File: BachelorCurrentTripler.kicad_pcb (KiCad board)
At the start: 4 copper layers, 153.3 x 77.8 mm, 80 parts, among them J1 Conn_01x07_Pin, J2 Conn_01x01_Pin, J3 Conn_01x01_Pin, J5 Conn_01x01_Pin, J6 Conn_01x01_Pin, J7 Conn_01x01_Pin, Q10 IRLR8726EBF, Q11 IRLR8726EBF, Q13 C2M0025120D, Q14 C2M0025120D, Q15 C2M0025120D, Q16 C2M0025120D, Q7 C2M0025120D, Q8 C2M0025120D, Q9 IRLR8726EBF, U1 STDriveG600, U2 STDriveG600, U3 STDriveG600, U4 FAN3268, U5 FAN3268, U6 FAN3268

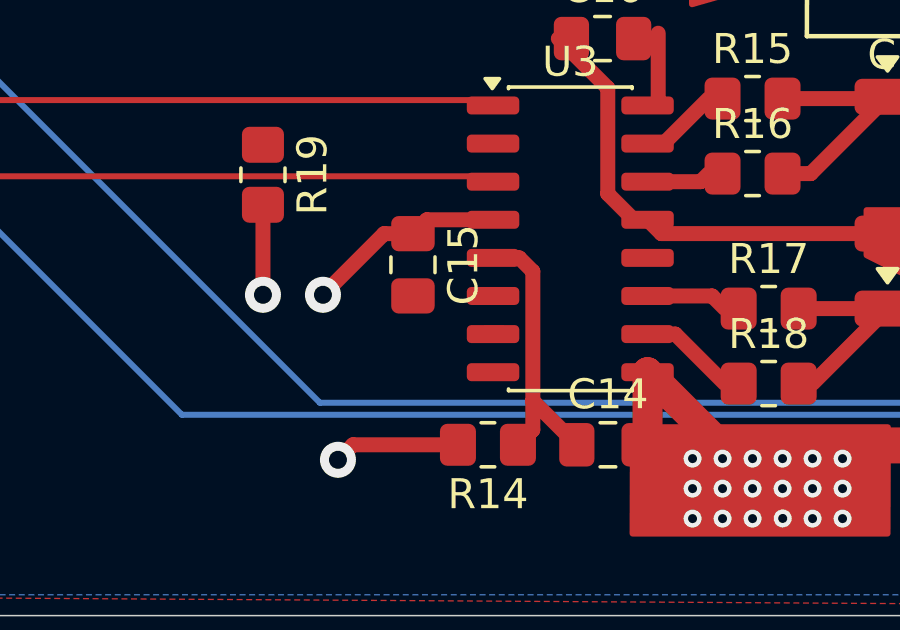
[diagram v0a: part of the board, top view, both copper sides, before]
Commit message: Small addition to GND on primary side
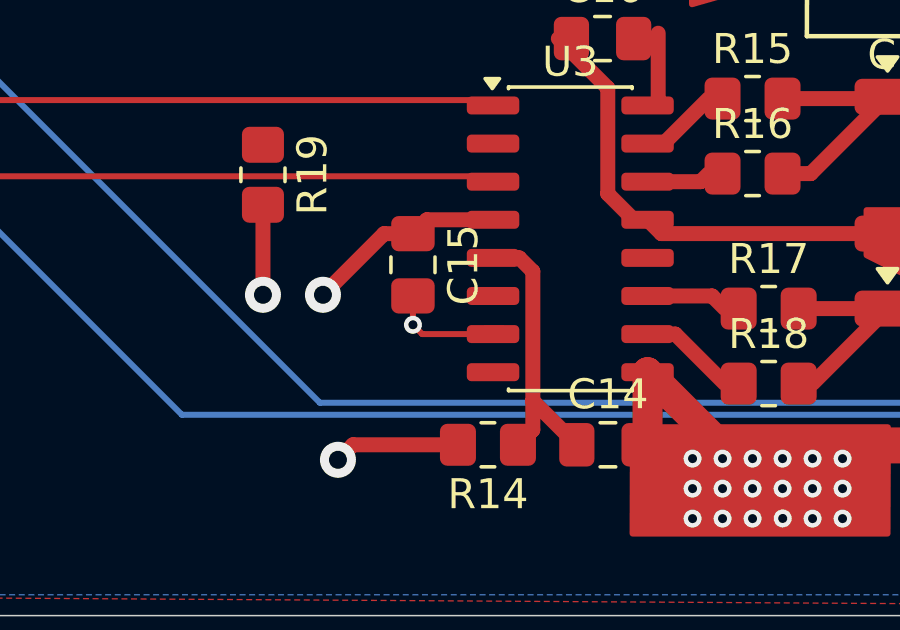
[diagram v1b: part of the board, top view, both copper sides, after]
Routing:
- net GND: track 53.8 -> 57.6 mm, vias 125 -> 126
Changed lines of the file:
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@@
+	)
+	(segment
+		(start 117.81 133.81)
+		(end 120.17 133.81)
+		(width 0.2)
+		(layer "F.Cu")
+		(net 1)
 	)
 	(segment
@@
 	)
 	(segment
+		(start 117.5 133.5)
+		(end 117.5 132.5375)
+		(width 0.2)
+		(layer "F.Cu")
+		(net 1)
+	)
+	(segment
 		(start 207.5375 120.5375)
 		(end 208.5 121.5)
@@
 	)
 	(segment
+		(start 117.5 133.5)
+		(end 117.81 133.81)
+		(width 0.2)
+		(layer "F.Cu")
+		(net 1)
+	)
+	(segment
 		(start 207.5375 120.5)
 		(end 207.5375 120.5375)
@@
 		(size 0.6)
 		(drill 0.3)
+		(layers "F.Cu" "B.Cu")
+		(net 1)
+	)
+	(via
+		(at 117.5 133.5)
+		(size 0.6)
+		(drill 0.3)

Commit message: Secondary side finished
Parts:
- added C36: C, Capacitor_THT:CP_Radial_D8.0mm_P5.00mm, F.Cu at (105.5, 91.5)
- added C37: C, Capacitor_THT:CP_Radial_D8.0mm_P5.00mm, F.Cu at (105.5, 77.6)
- moved C21 36.2 mm to (214.0, 116.6), turned to -90 degrees
- moved C26 34.3 mm to (202.0, 121.5), turned to -90 degrees
- moved C24 33.1 mm to (204.0, 121.5), turned to -90 degrees
- moved C23 27.9 mm to (202.0, 106.5), turned to -90 degrees
- moved C22 26.4 mm to (204.0, 106.5), turned to -90 degrees
- moved C20 18.9 mm to (214.0, 101.6), turned to -90 degrees
- moved C28 11.8 mm to (223.0, 102.6), turned to -90 degrees
- moved J3 11.5 mm to (91.0, 96.5)
- moved C25 10.4 mm to (204.0, 91.5), turned to -90 degrees
- moved C27 10.3 mm to (202.0, 91.5), turned to -90 degrees
- moved J5 9.05 mm to (91.5, 85.5)
- moved C29 7.83 mm to (214.5, 86.1), turned to -90 degrees
- moved C33 2.00 mm to (208.0, 90.5)
- moved C30 1.50 mm to (208.0, 92.5)
- moved R21 1.41 mm to (202.5, 112.5), turned to 180 degrees
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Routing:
- net /PhaseA/ALin: track 45.6 -> 226.2 mm, vias 0 -> 1
- net +12V: track 191.2 -> 337.7 mm, vias 29 -> 35
- net +1V2: track 0.00 -> 112.2 mm
- net /PhaseB/BLIN: track 147.9 -> 189.8 mm, vias 0 -> 1
- net /PhaseC/CLIN: track 142.2 -> 173.6 mm, vias 0 -> 1
- net /SecondarySide/SecA: track 27.9 -> 55.9 mm
- net /SecondarySide/SecB: track 5.00 -> 28.8 mm
- net GND: track 57.6 -> 34.3 mm, vias 126 -> 279
- net /PhaseC/COUT: track 47.4 -> 70.3 mm
- net /SecondarySide/SecC: track 5.00 -> 25.3 mm
- net /PhaseB/BOUT: track 35.2 -> 53.7 mm
- net /PhaseA/AOUT: track 59.7 -> 67.5 mm
- net /PhaseA/AHin: track 44.1 -> 51.7 mm
- net +48V: track 192.1 -> 195.0 mm
- net Net-(U4-OUTA): track 4.47 -> 2.48 mm
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
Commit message: Rettelser efter møde med Andreas
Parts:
- added H1: MountingHole_Pad, MountingHole:MountingHole_4.3mm_M4_Pad_Via, F.Cu at (227.8, 73.2)
- added H2: MountingHole_Pad, MountingHole:MountingHole_4.3mm_M4_Pad_Via, F.Cu at (227.8, 136.2)
- added H3: MountingHole_Pad, MountingHole:MountingHole_4.3mm_M4_Pad_Via, F.Cu at (113.5, 70.2)
- added H4: MountingHole_Pad, MountingHole:MountingHole_4.3mm_M4_Pad_Via, F.Cu at (92.0, 136.2)
- Q10, Q11, Q9: moved to B.Cu
- moved Q9 6.65 mm to (200.6, 96.5), turned to 0 degrees
- moved Q11 6.40 mm to (200.5, 124.7), turned to 0 degrees
- moved Q10 5.91 mm to (200.1, 110.2), turned to 0 degrees
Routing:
- net /SecondarySide/SecA: track 55.9 -> 82.1 mm, vias 0 -> 21
- net /SecondarySide/SecC: track 25.3 -> 34.1 mm, vias 0 -> 11
- net Net-(Q10-G): track 2.30 -> 6.47 mm, vias 0 -> 1
- net Net-(Q9-G): track 2.61 -> 6.39 mm, vias 0 -> 1
- net /PhaseA/ALin: track 226.2 -> 222.5 mm
- net Net-(Q11-G): track 2.57 -> 6.00 mm, vias 0 -> 1
- net /SecondarySide/SecB: track 28.8 -> 32.2 mm, vias 0 -> 18
- net /PhaseB/BLIN: track 189.8 -> 186.8 mm
- net GND: track 34.3 -> 33.5 mm, vias 279 -> 274
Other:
- outline, holes or cut-outs redrawn
- board text added: "0 mm"
- board text added: "10 mm"
- board text added: "20 mm"
- board text added: "30 mm"
- board text added: "40 mm"
- board text added: "HUSK PUNKT TIL FEEDBACK SPÆNDING"
- board text removed: "kør ikke strøm under"

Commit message: burde være færdig nu
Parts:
- added J8: Conn_01x02_Pin, Connector:JWT_A3963_1x02_P3.96mm_Vertical, F.Cu at (214.1, 136.5)
- moved H3 0.56 mm to (113.5, 70.8)
- moved R12 0.17 mm to (116.0, 106.2)
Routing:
- net +1V2: track 112.2 -> 148.4 mm
- net Net-(U3-SD): track 0.19 -> 7.88 mm
- net GND: track 33.5 -> 35.5 mm, vias 274 -> 286
- net /SecondarySide/SecC: vias 11 -> 12
- net +48V: vias 117 -> 115
- added copper zone on F.Cu, net +1V2
- added copper zone on B.Cu, net /SecondarySide/SecA
- added copper zone on F.Cu, net /SecondarySide/SecA
- added copper zone on B.Cu, net /SecondarySide/SecB
- added copper zone on B.Cu, net /SecondarySide/SecC
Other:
- board text added: "Vsense"
- board text removed: "J2"
- board text removed: "Stor kondensator mellem 48V og GND men også 12V og GND"
- board text removed: "byt"

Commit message: tilføj lige sidste markeringer
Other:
- board text added: "1V2"
- board text added: "AH"
- board text added: "AL"
- board text added: "BH"
- board text added: "BL"
- board text added: "CH"
- board text added: "CL"
- board text removed: "HUSK PUNKT TIL FEEDBACK SPÆNDING"
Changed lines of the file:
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@@
 		(embedded_fonts no)
 		(model "${KICAD9_3DMODEL_DIR}/Transformer_THT.3dshapes/Transformer_Breve_TEZ-47x57.step"
+			(hide yes)
 			(offset
 				(xyz 0 0 0)
@@
 		(tags "connector JST EH vertical")
 		(property "Reference" "J1"
-			(at 7.5 -2.8 90)
+			(at 7.5 3.3 90)
 			(layer "F.SilkS")
 			(effects
@@
 		(layer "Edge.Cuts")
 	)
-	(gr_text "HUSK PUNKT TIL FEEDBACK SPÆNDING"
-		(at 239.5 94 0)
-		(layer "F.Cu")
+	(gr_text "20 mm"
+		(at 186 75 270)
+		(layer "F.SilkS")
 		(effects
 			(font
-				(size 1.5 1.5)
-				(thickness 0.3)
-				(bold yes)
+				(size 1 1)
+				(thickness 0.1)
 			)
 			(justify left bottom)
 		)
 	)
-	(gr_text "20 mm"
-		(at 186 75 270)
+	(gr_text "AL"
+		(at 93 108 0)
+		(layer "F.SilkS")
+		(effects
+			(font
+				(size 1 1)
+				(thickness 0.1)
+			)
+			(justify left bottom)
+		)
+	)
+	(gr_text "AH"
+		(at 93 110.5 0)
 		(layer "F.SilkS")
 		(effects
@@
 		)
 	)
+	(gr_text "BL"
+		(at 93 113 0)
+		(layer "F.SilkS")
+		(effects
+			(font
+				(size 1 1)
+				(thickness 0.1)
+			)
+			(justify left bottom)
+		)
+	)
 	(gr_text "30 mm"
 		(at 196 75 270)
@@
 		)
 	)
+	(gr_text "CH"
+		(at 93 120.5 0)
+		(layer "F.SilkS")
+		(effects
+			(font
+				(size 1 1)
+				(thickness 0.1)
+			)
+			(justify left bottom)
+		)
+	)
+	(gr_text "1V2"
+		(at 230 96 0)
+		(layer "F.SilkS")
+		(effects
+			(font
+				(size 2 2)
+				(thickness 0.1)
+			)
+			(justify left bottom)
+		)
+	)
+	(gr_text "GND"
+		(at 93 123 0)
+		(layer "F.SilkS")
+		(effects
+			(font
+				(size 1 1)
+				(thickness 0.1)
+			)
+			(justify left bottom)
+		)
+	)
+	(gr_text "CL"
+		(at 93 118 0)
+		(layer "F.SilkS")
+		(effects
+			(font
+				(size 1 1)
+				(thickness 0.1)
+			)
+			(justify left bottom)
+		)
+	)
 	(gr_text "10-15V max"
 		(at 87 93.5 0)
@@
 		)
 	)
+	(gr_text "BH"
+		(at 93 115.5 0)
+		(layer "F.SilkS")
+		(effects
+			(font
+				(size 1 1)
+				(thickness 0.1)
+			)
+			(justify left bottom)
+		)
+	)
 	(gr_text "40 mm"
 		(at 206 75 270)
@@
 				(thickness 0.1)
 			)
+			(justify left bottom)
+		)
+	)
+	(gr_text "GND"
+		(at 229.5 114.5 0)
+		(layer "F.SilkS")
+		(effects
+			(font
+				(size 2 2)
+				(thickness 0.1)
+			)

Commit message: Final Value Changes
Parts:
- C20, C29: value 220u -> 100u
- C28: value 100u -> 220u
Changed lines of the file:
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@@
 			)
 		)
-		(property "Value" "220u"
+		(property "Value" "100u"
 			(at -4 0 90)
 			(layer "F.Fab")
@@
 			)
 		)
-		(property "Value" "220u"
+		(property "Value" "100u"
 			(at 2.5 5.25 90)
 			(layer "F.Fab")
@@
 			)
 		)
-		(property "Value" "100u"
+		(property "Value" "220u"
 			(at 2.5 5.25 90)
 			(layer "F.Fab")
@@
 		(min_thickness 0.25)
 		(filled_areas_thickness no)
-		(fill yes
+		(fill
 			(thermal_gap 0.5)
 			(thermal_bridge_width 0.5)
@@
 		(min_thickness 0.25)
 		(filled_areas_thickness no)
-		(fill yes
+		(fill
 			(thermal_gap 0.5)
 			(thermal_bridge_width 0.5)
@@
 		(min_thickness 0.25)
 		(filled_areas_thickness no)
-		(fill yes
+		(fill
 			(thermal_gap 0.5)
 			(thermal_bridge_width 0.5)
@@
 		(min_thickness 0.25)
 		(filled_areas_thickness no)
-		(fill yes
+		(fill
 			(thermal_gap 0.5)
 			(thermal_bridge_width 0.5)
@@
 		(min_thickness 0.25)
 		(filled_areas_thickness no)
-		(fill yes
+		(fill
 			(thermal_gap 0.5)
 			(thermal_bridge_width 0.5)
@@
 		(min_thickness 0.25)
 		(filled_areas_thickness no)
-		(fill yes
+		(fill
 			(thermal_gap 0.5)
 			(thermal_bridge_width 0.5)
@@
 		(min_thickness 0.25)
 		(filled_areas_thickness no)
-		(fill yes
+		(fill
 			(thermal_gap 0.5)
 			(thermal_bridge_width 0.5)
@@
 		(min_thickness 0.25)
 		(filled_areas_thickness no)
-		(fill yes
+		(fill
 			(thermal_gap 0.5)
 			(thermal_bridge_width 0.5)
@@
 		(min_thickness 0.25)
 		(filled_areas_thickness no)
-		(fill yes
+		(fill
 			(thermal_gap 0.5)
 			(thermal_bridge_width 0.5)
@@
 		(min_thickness 0.25)
 		(filled_areas_thickness no)
-		(fill yes
+		(fill
 			(thermal_gap 0.5)
 			(thermal_bridge_width 0.5)
@@
 		(min_thickness 0.25)
 		(filled_areas_thickness no)
-		(fill yes
+		(fill
 			(thermal_gap 0.5)
 			(thermal_bridge_width 0.5)
@@
 		(min_thickness 0.25)
 		(filled_areas_thickness no)
-		(fill yes
+		(fill
 			(thermal_gap 0.5)
 			(thermal_bridge_width 0.5)
